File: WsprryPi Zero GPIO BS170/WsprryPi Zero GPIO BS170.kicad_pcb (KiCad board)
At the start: 2 copper layers, 65 x 30 mm, 28 parts, among them J12 Conn_01x03, J41 SMA_Adafruit_1865, J42 J81/J82 LPF sockets, SW11 SKRPANE010, T21 WBC2-1TLC, T41 WBC2-1TLC, U11 Raspberry Pi 40-pin HAT inter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, U31 LTC6432AIUF-15#PBF, U51 TPS22918DBVR

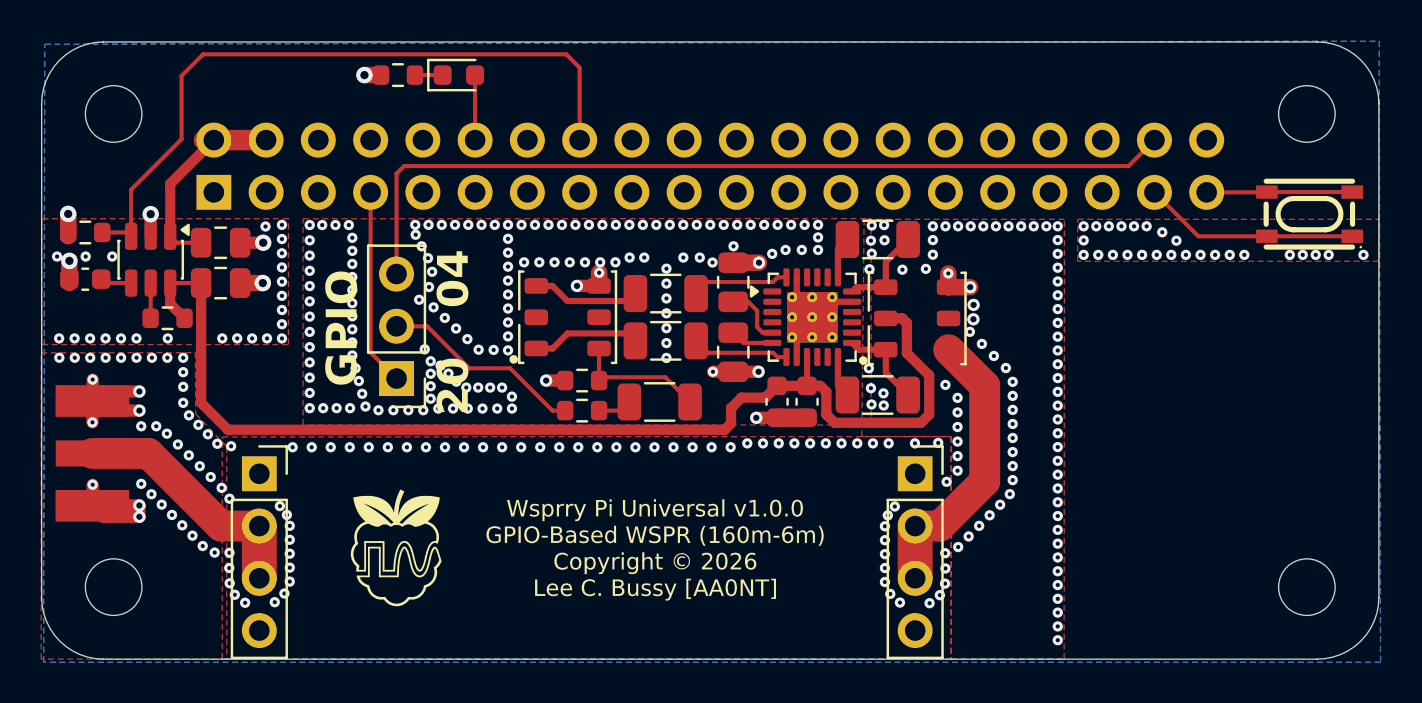
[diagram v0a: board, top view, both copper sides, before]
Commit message: Universal GPIO wBS170
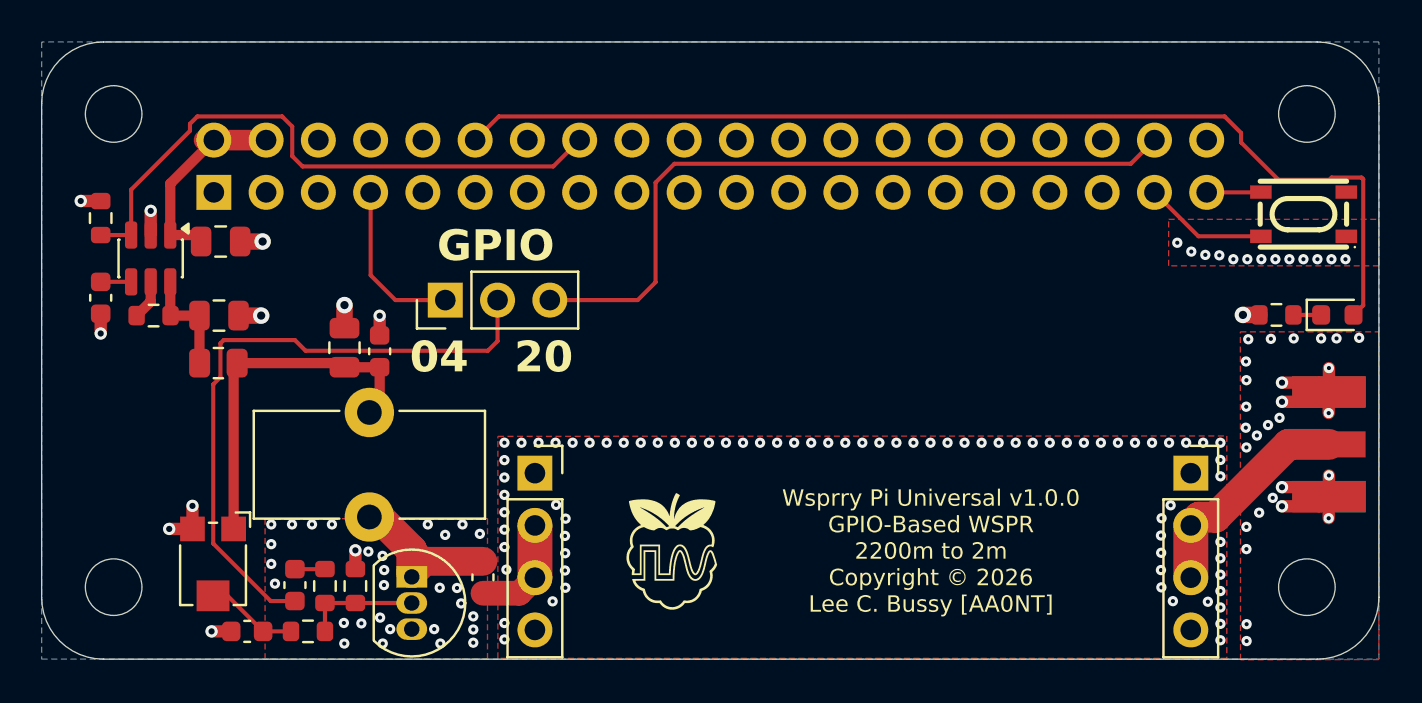
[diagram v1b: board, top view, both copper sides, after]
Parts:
- removed C33, C34: 1µF, wsprrypi-zero-gpio-bs170:C_0805_2012Metric
- removed C35: 100nF, wsprrypi-zero-gpio-bs170:C_0603_1608Metric
- removed C36: 1nF, wsprrypi-zero-gpio-bs170:C_0603_1608Metric
- removed C37, C38: 1µF, wsprrypi-zero-gpio-bs170:C_1206_3216Metric
- removed H1: Raspberry_Pi_HAT_2x20_Socket_3D, wsprrypi-zero-gpio-bs170:Raspberry_Pi_HAT_2x20_Socket_3D
- removed T21, T41: WBC2-1TLC, wsprrypi-zero-gpio-bs170:Coilcraft_WBC2-1TLC
- removed U31: LTC6432AIUF-15#PBF, wsprrypi-zero-gpio-bs170:Analog_UF24_QFN-24-1EP_4x4mm_P0.5mm_EP2.45x2.45mm_ThermalVias
- added C22: 100nF, wsprrypi-zero-gpio-bs170:C_0603_1608Metric, F.Cu at (110.0, 98.7)
- added C41: 100nF, wsprrypi-zero-gpio-bs170:C_0603_1608Metric, F.Cu at (121.5, 96.0)
- added L31: 25T FT37-43, wsprrypi-zero-gpio-bs170:L_Toroid_FT37-43_Vertical_P5.08mm, F.Cu at (115.9, 88.0)
- added Q31: BS170, wsprrypi-zero-gpio-bs170:TO-92_Inline, F.Cu at (118.0, 96.0)
- added R23: 100kΩ, wsprrypi-zero-gpio-bs170:R_0603_1608Metric, F.Cu at (115.2, 96.4)
- added R31: 0Ω, wsprrypi-zero-gpio-bs170:R_0805_2012Metric, F.Cu at (108.6, 85.6)
- added RV21: 5kΩ, wsprrypi-zero-gpio-bs170:Potentiometer_Bourns_TC33X_Vertical, F.Cu at (108.3, 95.5)
- C21, C31: value 1µF -> 100nF; footprint wsprrypi-zero-gpio-bs170:C_1206_3216Metric -> wsprrypi-zero-gpio-bs170:C_0603_1608Metric
- C32: footprint wsprrypi-zero-gpio-bs170:C_1206_3216Metric -> wsprrypi-zero-gpio-bs170:C_0805_2012Metric
- R22: value 100kΩ -> 4.7kΩ
- moved J41 64.7 mm to (164.9, 89.6), turned to 90 degrees
- moved R11 44.3 mm to (160.0, 83.3)
- moved D11 44.3 mm to (163.0, 83.3)
- moved C21 19.8 mm to (112.3, 96.4), turned to 90 degrees
- moved R22 18.1 mm to (112.9, 98.7)
- moved C32 15.8 mm to (114.7, 84.9), turned to -90 degrees
- moved R21 15.1 mm to (113.8, 96.4), turned to -90 degrees
- moved C31 13.9 mm to (116.4, 85.0), turned to -90 degrees
- moved J42 13.4 mm to (139.9, 91.0)
- moved J12 4.49 mm to (119.6, 82.5), turned to 90 degrees
- moved C53 1.58 mm to (108.6, 83.3)
- moved C52 1.18 mm to (102.9, 82.4), turned to -90 degrees
- moved R51 1.03 mm to (102.9, 78.6), turned to 90 degrees
- moved R52 0.69 mm to (105.4, 83.3)
- moved SW11 0.29 mm to (161.3, 78.4)
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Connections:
- C21 pad 1: Net-(C21-Pad1) -> /GPIO_RF
- C21 pad 2: Net-(T21-PRI1) -> Net-(C21-Pad2)
- C31 pad 1: /RF_DIFF_N -> GND
- C31 pad 2: Net-(U31--IN) -> /PRE_CHOKE
- C32 pad 1: /RF_DIFF_P -> GND
- C32 pad 2: Net-(U31-+IN) -> /PRE_CHOKE
- J42 pad 2: /FINAL_OUT -> /TX_OUT
- J42 pad 3: /FINAL_OUT -> /TX_OUT
- J42 pad 6: /TX_OUT -> /FINAL_OUT
- J42 pad 7: /TX_OUT -> /FINAL_OUT
- R21 pad 1: /GPIO_RF -> Net-(C21-Pad2)
- R21 pad 2: Net-(C21-Pad1) -> /GATE
- R22 pad 1: GND -> Net-(C22-Pad2)
- R22 pad 2: Net-(T21-PRI1) -> /GATE
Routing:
- net /SW_5V: track 55.5 -> 5.39 mm
- net /LED: track 3.16 -> 52.1 mm
- net /GPIO_RF: track 9.89 -> 30.9 mm
- net /PRE_CHOKE: track 0.00 -> 17.8 mm
- net GND: track 40.2 -> 29.1 mm, vias 387 -> 158
- net /TX_OUT: track 13.9 -> 5.38 mm
- net /PA_DRAIN: track 0.00 -> 7.51 mm
- net /GPIO20: track 42.4 -> 35.5 mm
- net Net-(T21-PRI1): track 6.57 -> 0.00 mm
- net /GATE: track 0.00 -> 5.60 mm
- net /RF_DIFF_P: track 5.27 -> 0.00 mm
- net /RF_DIFF_N: track 5.27 -> 0.00 mm
- net Net-(U31-+IN): track 4.72 -> 0.00 mm
- net Net-(U31--IN): track 4.72 -> 0.00 mm
- net Net-(C22-Pad2): track 0.00 -> 4.51 mm
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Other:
- board text added: "Wsprry Pi Universal v1.0.0 GPIO-Based WSPR 2200m to 2m Copyright © 2026 Lee C. Bussy [AA0NT]"
- board text removed: "Wsprry Pi Universal v1.0.0 GPIO-Based WSPR (160m-6m) Copyright © 2026 Lee C. Bussy [AA0NT]"

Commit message: Remove old designs
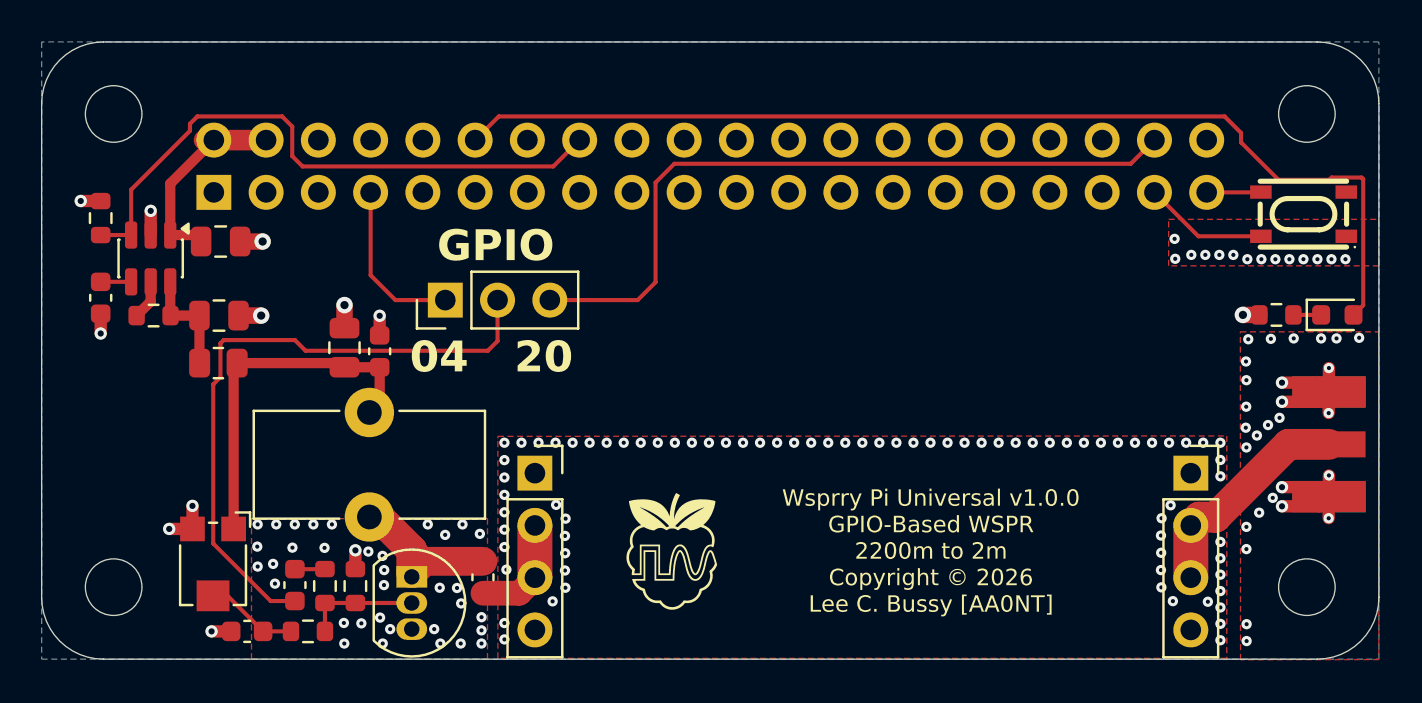
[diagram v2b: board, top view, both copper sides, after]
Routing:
- net GND: vias 158 -> 164
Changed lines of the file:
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@@
 	)
 	(via
+		(at 110.5 93.45)
+		(size 0.5)
+		(drill 0.2)
+		(layers "F.Cu" "B.Cu")
+		(free yes)
+		(net "GND")
+	)
+	(via
 		(at 114.11 93.45)
 		(size 0.5)
@@
 	)
 	(via
+		(at 155.1 80.54)
+		(size 0.5)
+		(drill 0.2)
+		(layers "F.Cu" "B.Cu")
+		(free yes)
+		(net "GND")
+	)
+	(via
 		(at 159.07 89.13)
 		(size 0.5)
@@
 	)
 	(via
+		(at 113.75 94.59)
+		(size 0.5)
+		(drill 0.2)
+		(layers "F.Cu" "B.Cu")
+		(free yes)
+		(net "GND")
+	)
+	(via
 		(at 162.94 84.41)
 		(size 0.5)
@@
 	)
 	(via
-		(at 120.98 97.92)
+		(at 121.38 97.96)
 		(size 0.5)
 		(drill 0.2)
@@
 	)
 	(via
-		(at 157.924792 80.56)
+		(at 157.924792 80.35)
 		(size 0.5)
 		(drill 0.2)
@@
 	)
 	(via
-		(at 120.98 98.56)
+		(at 121.38 98.6)
 		(size 0.5)
 		(drill 0.2)
@@
 	)
 	(via
-		(at 111.16 95.37)
+		(at 110.5 95.5)
+		(size 0.5)
+		(drill 0.2)
+		(layers "F.Cu" "B.Cu")
+		(free yes)
+		(net "GND")
+	)
+	(via
+		(at 111.25 95.37)
 		(size 0.5)
 		(drill 0.2)
@@
 	)
 	(via
-		(at 157.243594 80.37)
+		(at 157.243594 80.35)
 		(size 0.5)
 		(drill 0.2)
@@
 	)
 	(via
-		(at 113.14 93.45)
+		(at 113.2075 93.45)
 		(size 0.5)
 		(drill 0.2)
@@
 	)
 	(via
-		(at 155.881198 80.19)
+		(at 155.881198 80.35)
 		(size 0.5)
 		(drill 0.2)
@@
 	)
 	(via
-		(at 120.98 99.2)
+		(at 120.37 99.24)
+		(size 0.5)
+		(drill 0.2)
+		(layers "F.Cu" "B.Cu")
+		(free yes)
+		(net "GND")
+	)
+	(via
+		(at 121.38 99.24)
 		(size 0.5)
 		(drill 0.2)
@@
 	)
 	(via
-		(at 112.17 93.45)
+		(at 112.305 93.45)
 		(size 0.5)
 		(drill 0.2)
@@
 	)
 	(via
-		(at 111.16 93.45)
+		(at 111.4025 93.45)
 		(size 0.5)
 		(drill 0.2)
@@
 	)
 	(via
+		(at 110.48 94.53)
+		(size 0.5)
+		(drill 0.2)
+		(layers "F.Cu" "B.Cu")
+		(free yes)
+		(net "GND")
+	)
+	(via
 		(at 119.08 98.54)
 		(size 0.5)
@@
 	)
 	(via
-		(at 111.16 94.41)
+		(at 112.19 94.58)
 		(size 0.5)
 		(drill 0.2)
@@
 	)
 	(via
-		(at 155.2 79.76)
+		(at 155.07 79.57)
 		(size 0.5)
 		(drill 0.2)
@@
 		(layer "F.Cu")
 		(hatch none 0.1)
+		(priority 30048)
+		(attr
+			(teardrop
+				(type padvia)
+			)
+		)
+		(connect_pads yes
+			(clearance 0)
+		)
+		(min_thickness 0.0254)
+		(fill yes
+			(island_removal_mode 1)
+		)
+		(polygon
+			(pts
+				(xy 115.55 94.82) (xy 114.95 94.82) (xy 114.85 95.267606) (xy 115.25 95.621) (xy 115.65 95.267606)
+			)
+		)
+	)
+	(zone
+		(net "GND")
+		(layer "F.Cu")
+		(hatch none 0.1)
 		(priority 30008)
 		(attr
@@
 		(layer "F.Cu")
 		(hatch none 0.1)
-		(priority 30067)
+		(priority 30068)
 		(attr
 			(teardrop
@@
 		(layer "F.Cu")
 		(hatch none 0.1)
-		(priority 30054)
+		(priority 30055)
 		(attr
 			(teardrop
@@
 		(layer "F.Cu")
 		(hatch none 0.1)
-		(priority 30055)
+		(priority 30056)
 		(attr
 			(teardrop
@@
 		(layer "F.Cu")
 		(hatch none 0.1)
-		(priority 30056)
+		(priority 30057)
 		(attr
 			(teardrop
@@
 		(layer "F.Cu")
 		(hatch none 0.1)
-		(priority 30053)
+		(priority 30054)
 		(attr
 			(teardrop
@@
 		(layer "F.Cu")
 		(hatch none 0.1)
-		(priority 30060)
+		(priority 30061)
 		(attr
 			(teardrop
@@
 		(layer "F.Cu")
 		(hatch none 0.1)
-		(priority 30057)
+		(priority 30058)
 		(attr
 			(teardrop
@@
 		(layer "F.Cu")
 		(hatch none 0.1)
-		(priority 30058)
+		(priority 30059)
 		(attr
 			(teardrop
@@
 		(layer "F.Cu")
 		(hatch none 0.1)
-		(priority 30059)
+		(priority 30060)
 		(attr
 			(teardrop
@@
 		(layer "F.Cu")
 		(hatch none 0.1)
-		(priority 30050)
+		(priority 30051)
 		(attr
 			(teardrop
@@
 		(layer "F.Cu")
 		(hatch none 0.1)
-		(priority 30068)
+		(priority 30069)
 		(attr
 			(teardrop
@@
 		(layer "F.Cu")
 		(hatch none 0.1)
-		(priority 30051)
+		(priority 30052)
 		(attr
 			(teardrop
@@
 		(layer "F.Cu")
 		(hatch none 0.1)
-		(priority 30049)
+		(priority 30050)
 		(attr
 			(teardrop
@@
 		(layer "F.Cu")
 		(hatch none 0.1)
-		(priority 30066)
+		(priority 30067)
 		(attr
 			(teardrop
@@
 		(layer "F.Cu")
 		(hatch none 0.1)
-		(priority 30064)
+		(priority 30065)
 		(attr
 			(teardrop
@@
 		(layer "F.Cu")
 		(hatch none 0.1)
-		(priority 30052)
+		(priority 30053)
 		(attr
 			(teardrop
@@
 		(polygon
 			(pts
-				(xy 121.67 93.17) (xy 121.67 100) (xy 110.86 100) (xy 110.86 93.17)
+				(xy 121.67 93.17) (xy 121.67 100) (xy 110.2 100) (xy 110.2 93.17)
 			)
 		)
@@
 		(layer "F.Cu")
 		(hatch none 0.1)
-		(priority 30061)
+		(priority 30062)
 		(attr
 			(teardrop
@@
 		(layer "F.Cu")
 		(hatch none 0.1)
-		(priority 30048)
+		(priority 30049)
 		(attr
 			(teardrop
@@
 		(layer "F.Cu")
 		(hatch none 0.1)
-		(priority 30062)
+		(priority 30063)
 		(attr
 			(teardrop
@@
 		(layer "F.Cu")
 		(hatch none 0.1)
-		(priority 30065)
+		(priority 30066)
 		(attr
 			(teardrop
@@
 		(layer "F.Cu")
 		(hatch none 0.1)
-		(priority 30063)
+		(priority 30064)
 		(attr
 			(teardrop

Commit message: Header changed to match QRP Labs
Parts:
- moved RV21 3.71 mm to (107.0, 92.0)
- moved C31 1.81 mm to (114.6, 85.0)
- moved C32 1.81 mm to (112.9, 84.9)
- moved L31 1.31 mm to (114.6, 88.0)
- moved C21 1.31 mm to (111.0, 96.4)
- moved C22 1.31 mm to (108.7, 98.7)
- moved C41 1.31 mm to (120.1, 96.0)
- moved Q31 1.31 mm to (116.7, 96.0)
- moved R21 1.31 mm to (112.5, 96.4)
- moved R22 1.31 mm to (111.6, 98.7)
- moved R23 1.31 mm to (113.9, 96.4)
- moved J42 1.31 mm to (138.6, 91.0)
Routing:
- net /PRE_CHOKE: track 17.8 -> 12.8 mm
- net Net-(C22-Pad2): track 4.51 -> 7.56 mm
- net /GPIO_RF: track 30.9 -> 30.2 mm
- net GND: track 29.1 -> 28.9 mm, vias 164 -> 172

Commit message: Renumber BS170 functional blocks and component references
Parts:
- renumbered C51 to C21, C52 to C22, C53 to C23, C21 to C31, C22 to C32, C31 to C41, C32 to C42, C41 to C51, J41 to J51, J42 to J52, L31 to L41, Q31 to Q41, R51 to R21, R52 to R22, R21 to R31, R22 to R32, R23 to R33, R31 to R41, RV21 to RV31, U51 to U21

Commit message: File rename and cleanup
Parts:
- J52: value J81/J82 LPF sockets -> LPF female headers; footprint wsprrypi-zero-gpio-bs170:Dual_PinSocket_1x04_P2.54mm_J81_J82 -> wsprrypi-zero-gpio-bs170:LPF_HeaderPair_Female_2x1x04_P2.54mm_S33.02mm
- turned C51 to -90 degrees
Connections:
- C51 pad 1: /TX_OUT -> /PA_DRAIN
- C51 pad 2: /PA_DRAIN -> /FINAL_OUT
- J51 pad 1: /FINAL_OUT -> /TX_OUT
- J52 pad 2: /TX_OUT -> /FINAL_OUT
- J52 pad 3: /TX_OUT -> /FINAL_OUT
- J52 pad 6: /FINAL_OUT -> /TX_OUT
- J52 pad 7: /FINAL_OUT -> /TX_OUT
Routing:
- net /TX_OUT: track 5.38 -> 11.1 mm
- net /FINAL_OUT: track 11.1 -> 5.38 mm
- net /PA_DRAIN: track 7.51 -> 11.2 mm
- net GND: vias 172 -> 171

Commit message: Add bias set
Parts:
- added J21: BIAS_SET, wsprrypi-zero-gpio-bs170:PinHeader_1x02_P2.54mm_Vertical, F.Cu at (117.3, 82.1)
- J12: value Conn_01x03 -> GPIO
- moved J12 3.82 mm to (123.4, 82.1)
- turned C21 to 0 degrees
- turned C41 to 90 degrees
- turned C42 to 90 degrees
- turned R22 to 180 degrees
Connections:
- C21 pad 1: GND -> /PI_5V
- C21 pad 2: /PI_5V -> GND
- C41 pad 1: GND -> /BIAS
- C41 pad 2: /PRE_CHOKE -> GND
- C42 pad 1: GND -> /BIAS
- C42 pad 2: /PRE_CHOKE -> GND
- L41 pad 1: /PRE_CHOKE -> /BIAS
- R22 pad 1: Net-(U21-QOD) -> /SW_5V
- R22 pad 2: /SW_5V -> Net-(U21-QOD)
- R41 pad 2: /PRE_CHOKE -> /BIAS
- RV31 pad 1: /PRE_CHOKE -> /BIAS
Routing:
- net /SW_5V: track 5.39 -> 19.6 mm
- net /PRE_CHOKE: track 12.8 -> 0.00 mm
- net /BIAS: track 0.00 -> 12.8 mm
- net /PI_5V: track 10.6 -> 21.8 mm
- net /GPIO20: track 35.5 -> 30.9 mm
- net /GPIO_RF: track 30.2 -> 34.2 mm
- net /GPIO4: track 8.16 -> 9.39 mm
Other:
- board text removed: "GPIO"

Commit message: Update with part selections
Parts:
- D11: value KT-0603W -> KT-0603R
